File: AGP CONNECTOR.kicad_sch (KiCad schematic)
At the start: 4 parts, among them J32 AGP2.0_GENERIC, U7 7407

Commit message: page 15 agp
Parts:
- removed U7: 7407, P2-3_ERA:NS14, symbol 74xx_IEEE:7407
- added U7: 74AS07, symbol P2-3_era:74AS07
- J32: value AGP2.0_GENERIC -> AGP_CONN_1.3
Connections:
- net AGP_OC#: no longer J32.A16 (VCC3.3), J32.A28 (VCC3.3), J32.A45 (VCC3.3), J32.A9 (VCC3.3), J32.B16 (VCC3.3), J32.B28 (VCC3.3), J32.B45 (VCC3.3), J32.B6 (INTB#), J32.B9 (VCC3.3), R56.2
- net PIRQ#A: now also U7.4
- net PIRQ#B: now also U7.6
- net USB_AGP-: now reaches J32.A4 (USB-)
- net at J32.A6 (INTA#), R55.2: now also U7.3
- net USB_AGP+: now reaches J32.B4 (USB+)
- net Earth renamed GND
- net GND: no longer J32.A13 (GND), J32.A19 (GND), J32.A31 (GND), J32.A37 (GND), J32.A43 (GND), J32.A49 (GND), J32.A5 (GND), J32.A55 (GND), J32.A61 (GND)
- new net: J32.B6 (INTB#), R56.2, U7.5
- new net: J32.A13 (GND), J32.A19 (GND), J32.A31 (GND), J32.A37 (GND), J32.A43 (GND), J32.A49 (GND), J32.A5 (GND), J32.A55 (GND), J32.A61 (GND)
- new net: J32.A16 (VCC3.3), J32.A28 (VCC3.3), J32.A45 (VCC3.3), J32.A9 (VCC3.3), J32.B16 (VCC3.3), J32.B28 (VCC3.3), J32.B45 (VCC3.3), J32.B9 (VCC3.3)
- no-connect marks 15 -> 13
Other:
- note removed: "removed"
- title: (none) -> ACCELERATED GRAPHICS PORT (AGP) CONNECTOR
- moved on the sheet: R55, R56

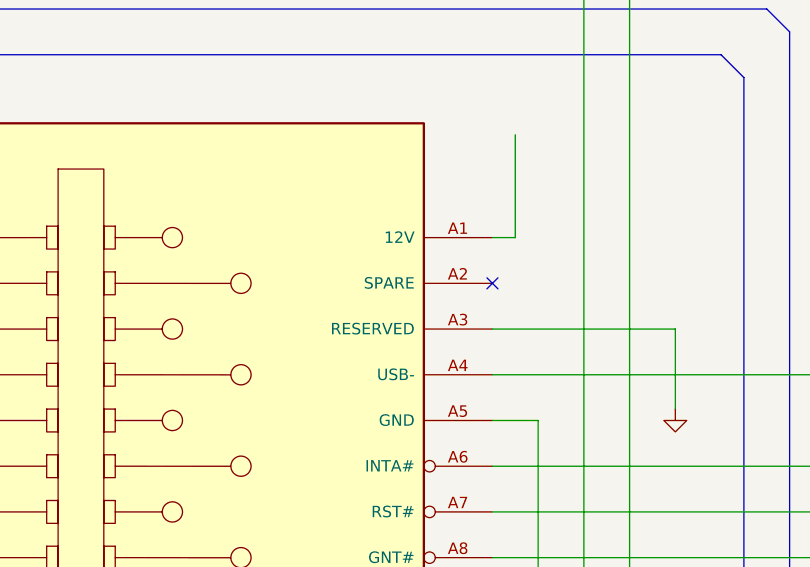
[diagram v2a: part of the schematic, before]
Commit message: Pages 16 17 PCI, tweaked page 15
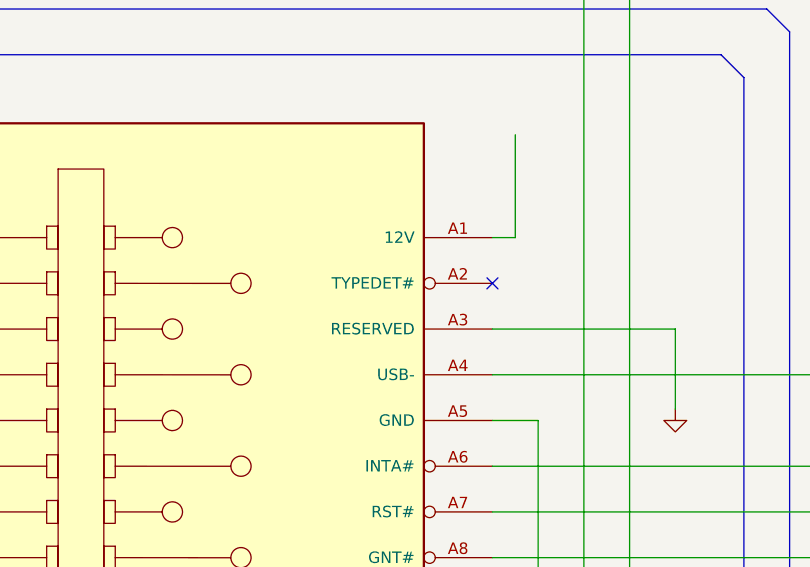
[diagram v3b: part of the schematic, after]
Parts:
- J32: symbol P2-3_era:AGP2.0_GENERIC -> P2-3_era:AGP1.0_Slot
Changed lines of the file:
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@@
 	)
 	(symbol
-		(lib_name "AGP2.0_GENERIC_1")
-		(lib_id "P2-3_era:AGP2.0_GENERIC")
+		(lib_id "P2-3_era:AGP1.0_Slot")
 		(at 292.1 238.76 0)
 		(unit 1)
@@
 		)
 		(property "Datasheet" "blah"
-			(at 247.65 64.77 0)
+			(at 263.652 115.062 0)
 			(effects
 				(font
@@
 		)
 		(property "Description" "blah"
-			(at 262.382 44.45 0)
+			(at 278.384 94.742 0)
 			(effects
 				(font

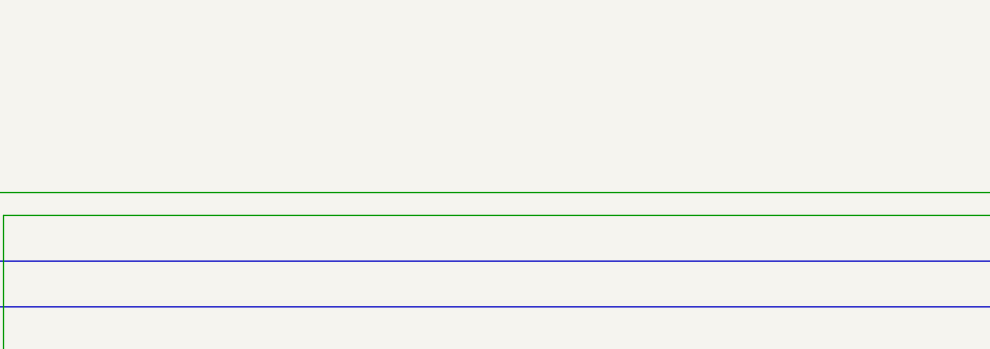
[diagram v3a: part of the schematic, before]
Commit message: page 18 ISA, small fixes
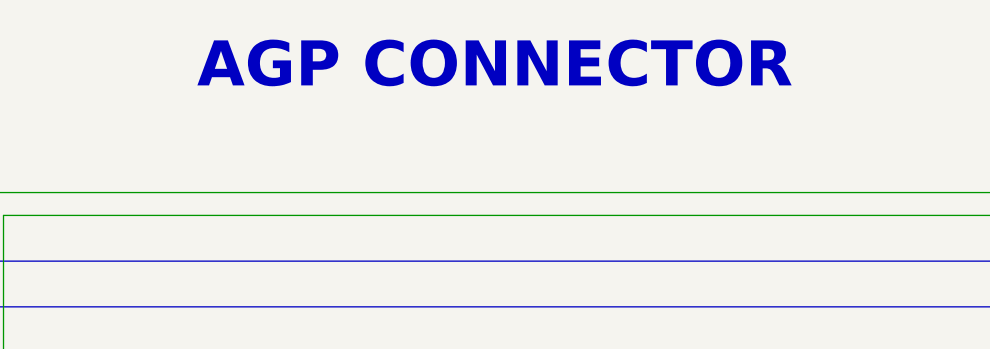
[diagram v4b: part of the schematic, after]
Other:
- note added: "AGP CONNECTOR"
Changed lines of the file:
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@@
 		(rev "1.0")
+	)
+	(text "AGP CONNECTOR"
+		(exclude_from_sim no)
+		(at 290.83 29.21 0)
+		(effects
+			(font
+				(size 5 5)
+				(thickness 0.6)
+				(bold yes)
+			)
+		)
 	)
 	(junction
